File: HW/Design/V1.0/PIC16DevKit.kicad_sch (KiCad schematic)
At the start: 0 parts

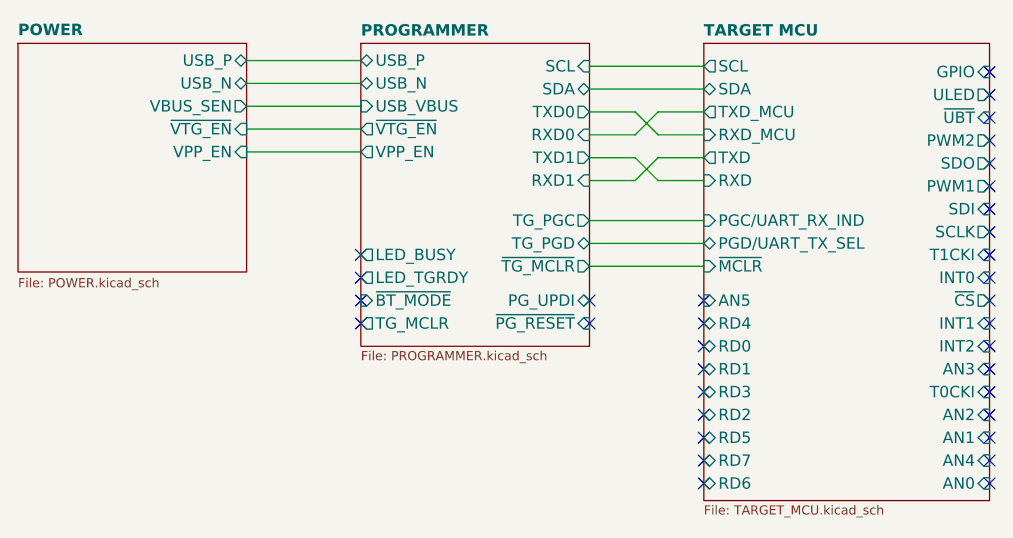
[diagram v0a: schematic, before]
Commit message: PCB V2: change programmer MCU
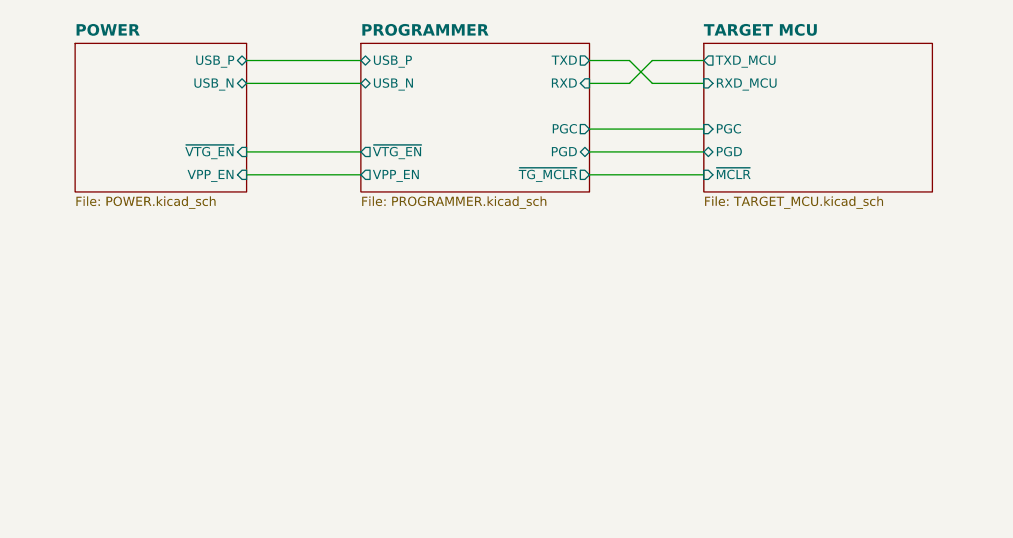
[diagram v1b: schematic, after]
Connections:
- no-connect marks 34 -> 0
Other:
- sheet POWER ports: added none; removed VBUS_SEN
- sheet PROGRAMMER ports: added PGC, PGD, RXD, TXD; removed LED_BUSY, LED_TGRDY, PG_UPDI, RXD0, RXD1, SCL, SDA, TG_MCLR, TG_PGC, TG_PGD, TXD0, TXD1, USB_VBUS, ~{BT_MODE}, ~{PG_RESET}
- sheet TARGET MCU ports: added PGC, PGD; removed AN0, AN1, AN2, AN3, AN4, AN5, GPIO, INT0, INT1, INT2, PGC/UART_RX_IND, PGD/UART_TX_SEL, PWM1, PWM2, RD0, RD1, RD2, RD3, RD4, RD5, RD6, RD7, RXD, SCL, SCLK, SDA, SDI, SDO, T0CKI, T1CKI, TXD, ULED, ~{CS}, ~{UBT}
